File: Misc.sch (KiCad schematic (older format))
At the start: 22 parts, among them U3 PCF8523TK, U4 TLV70218DBV, U5 CDCE913PW, U7 LM75BDP, U8 LM75BDP, X1 32768, X2 20MHz

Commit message: Switch resistors to 0402
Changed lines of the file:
@@
 	5000 2000 4900 2000
 Wire Wire Line
-	4900 2000 4900 2100
-Wire Wire Line
-	4900 2100 4900 2200
+	4900 2000 4900 2200
 Wire Wire Line
 	5000 2100 4900 2100
@@
 $EndComp
 Wire Wire Line
-	2000 1500 2100 1500
-Wire Wire Line
-	2100 1500 2450 1500
-Wire Wire Line
-	2450 1500 2800 1500
-Wire Wire Line
-	2800 1500 3150 1500
-Wire Wire Line
-	3150 1500 5000 1500
+	2000 1500 5000 1500
 $Comp
 L C-0402 C?
@@
 $EndComp
 Wire Wire Line
-	3800 1600 4300 1600
-Wire Wire Line
-	4300 1600 5000 1600
+	3800 1600 5000 1600
 Wire Wire Line
 	3800 1600 3800 1700
@@
 	6100 3900 6200 3900
 Wire Wire Line
-	6200 3900 6200 4000
-Wire Wire Line
-	6200 4000 6200 4100
+	6200 3900 6200 4100
 Wire Wire Line
 	6200 4000 6100 4000
@@
 $EndComp
 Wire Wire Line
-	4300 3800 4600 3800
-Wire Wire Line
-	4600 3800 5100 3800
+	4300 3800 5100 3800
 $Comp
 L GND #PWR169
@@
 	3600 3900 3500 3900
 Wire Wire Line
-	3500 3900 3500 3800
-Wire Wire Line
-	3000 3800 3100 3800
-Wire Wire Line
-	3100 3800 3400 3800
-Wire Wire Line
-	3400 3800 3500 3800
-Wire Wire Line
-	3500 3800 3600 3800
+	3500 3800 3500 3900
+Wire Wire Line
+	3000 3800 3600 3800
 Connection ~ 3500 3800
 Text GLabel 3000 3800 0    50   Input ~ 0
@@
 	3400 3800 3400 4300
 Wire Wire Line
-	3400 4300 5000 4300
+	5000 4300 3400 4300
 Wire Wire Line
 	5000 3900 5100 3900
@@
 	4600 4150 4600 4100
 Wire Wire Line
-	5000 4300 5000 4000
-Wire Wire Line
-	5000 4000 5000 3900
+	5000 3900 5000 4300
 $Comp
 L LM75BDP U7
@@
 P3V3_AUX
 Wire Wire Line
-	4700 4800 4800 4800
-Wire Wire Line
-	4800 4800 5200 4800
+	4700 4800 5200 4800
 Text HLabel 1600 2500 0    50   BiDi ~ 0
 SDA_S0
@@
 	1600 2500 2400 2500
 Wire Wire Line
-	2400 2500 2400 3400
-Wire Wire Line
-	2400 3400 2400 4900
-Wire Wire Line
-	2400 4900 2400 6200
-Wire Wire Line
-	2300 2600 2300 3500
-Wire Wire Line
-	2300 3500 2300 5000
-Wire Wire Line
-	2300 5000 2300 6300
+	2400 2500 2400 6200
+Wire Wire Line
+	2300 2600 2300 6300
 Wire Wire Line
 	2300 2600 1600 2600
@@
 $EndComp
 Wire Wire Line
-	5100 5100 5100 5200
-Wire Wire Line
-	5100 5200 5100 5300
-Wire Wire Line
-	5100 5300 5100 5400
-Wire Wire Line
-	5100 5400 5100 5500
+	5100 5100 5100 5500
 Wire Wire Line
 	5100 5100 5200 5100
@@
 P3V3_AUX
 Wire Wire Line
-	4700 6100 4800 6100
-Wire Wire Line
-	4800 6100 5100 6100
-Wire Wire Line
-	5100 6100 5200 6100
+	4700 6100 5200 6100
 Wire Wire Line
 	2400 6200 5200 6200
@@
 	5200 6500 5100 6500
 Wire Wire Line
-	5100 6500 5100 6600
-Wire Wire Line
-	5100 6600 5100 6700
-Wire Wire Line
-	5100 6700 5100 6800
+	5100 6500 5100 6800
 $Comp
 L GND #PWR176
@@
 	6600 3100 6100 3100
 Wire Wire Line
-	6800 3100 7200 3100
-Wire Wire Line
-	7200 3100 7400 3100
+	6800 3100 7400 3100
 $Comp
 L R-0402 R89
@@
 $EndComp
 Wire Wire Line
-	6800 3200 6900 3200
-Wire Wire Line
-	6900 3200 7400 3200
+	6800 3200 7400 3200
 Wire Wire Line
 	6600 3200 6100 3200

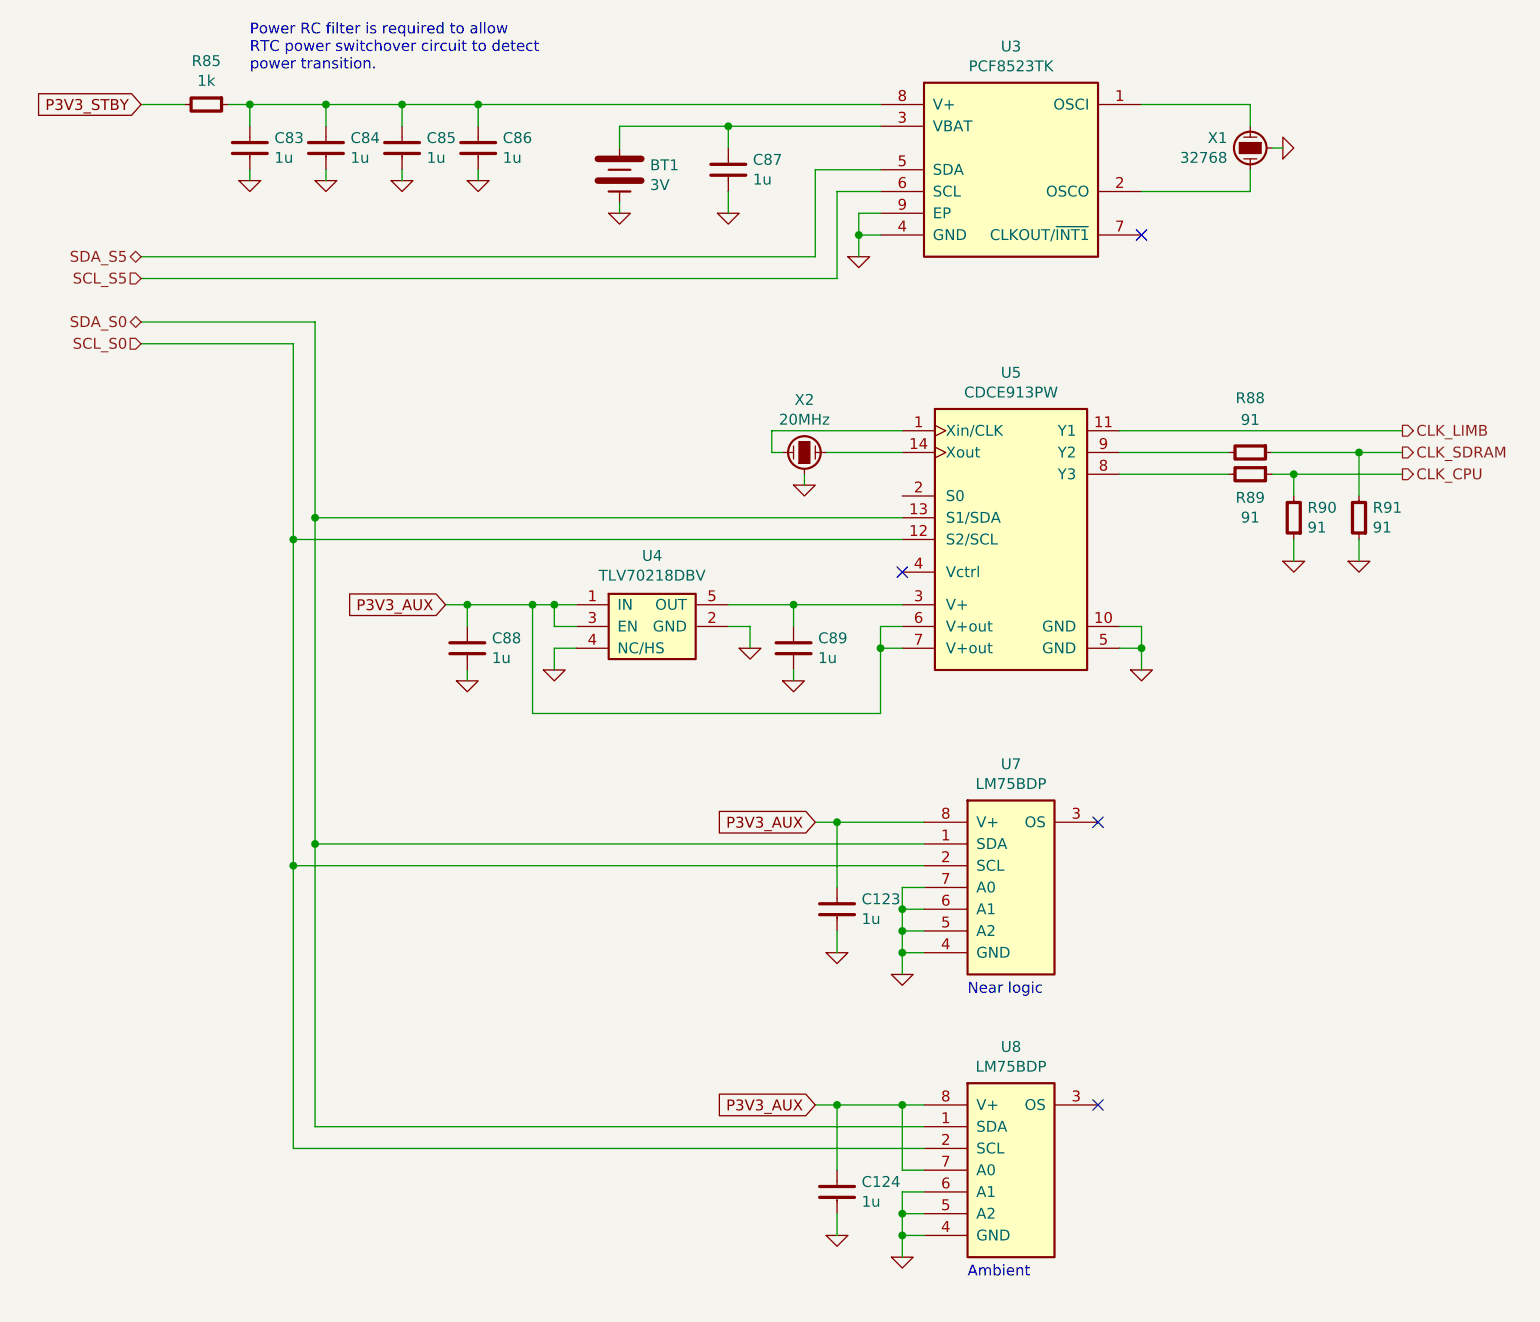
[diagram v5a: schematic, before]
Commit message: Gather and assign all I2C addresses
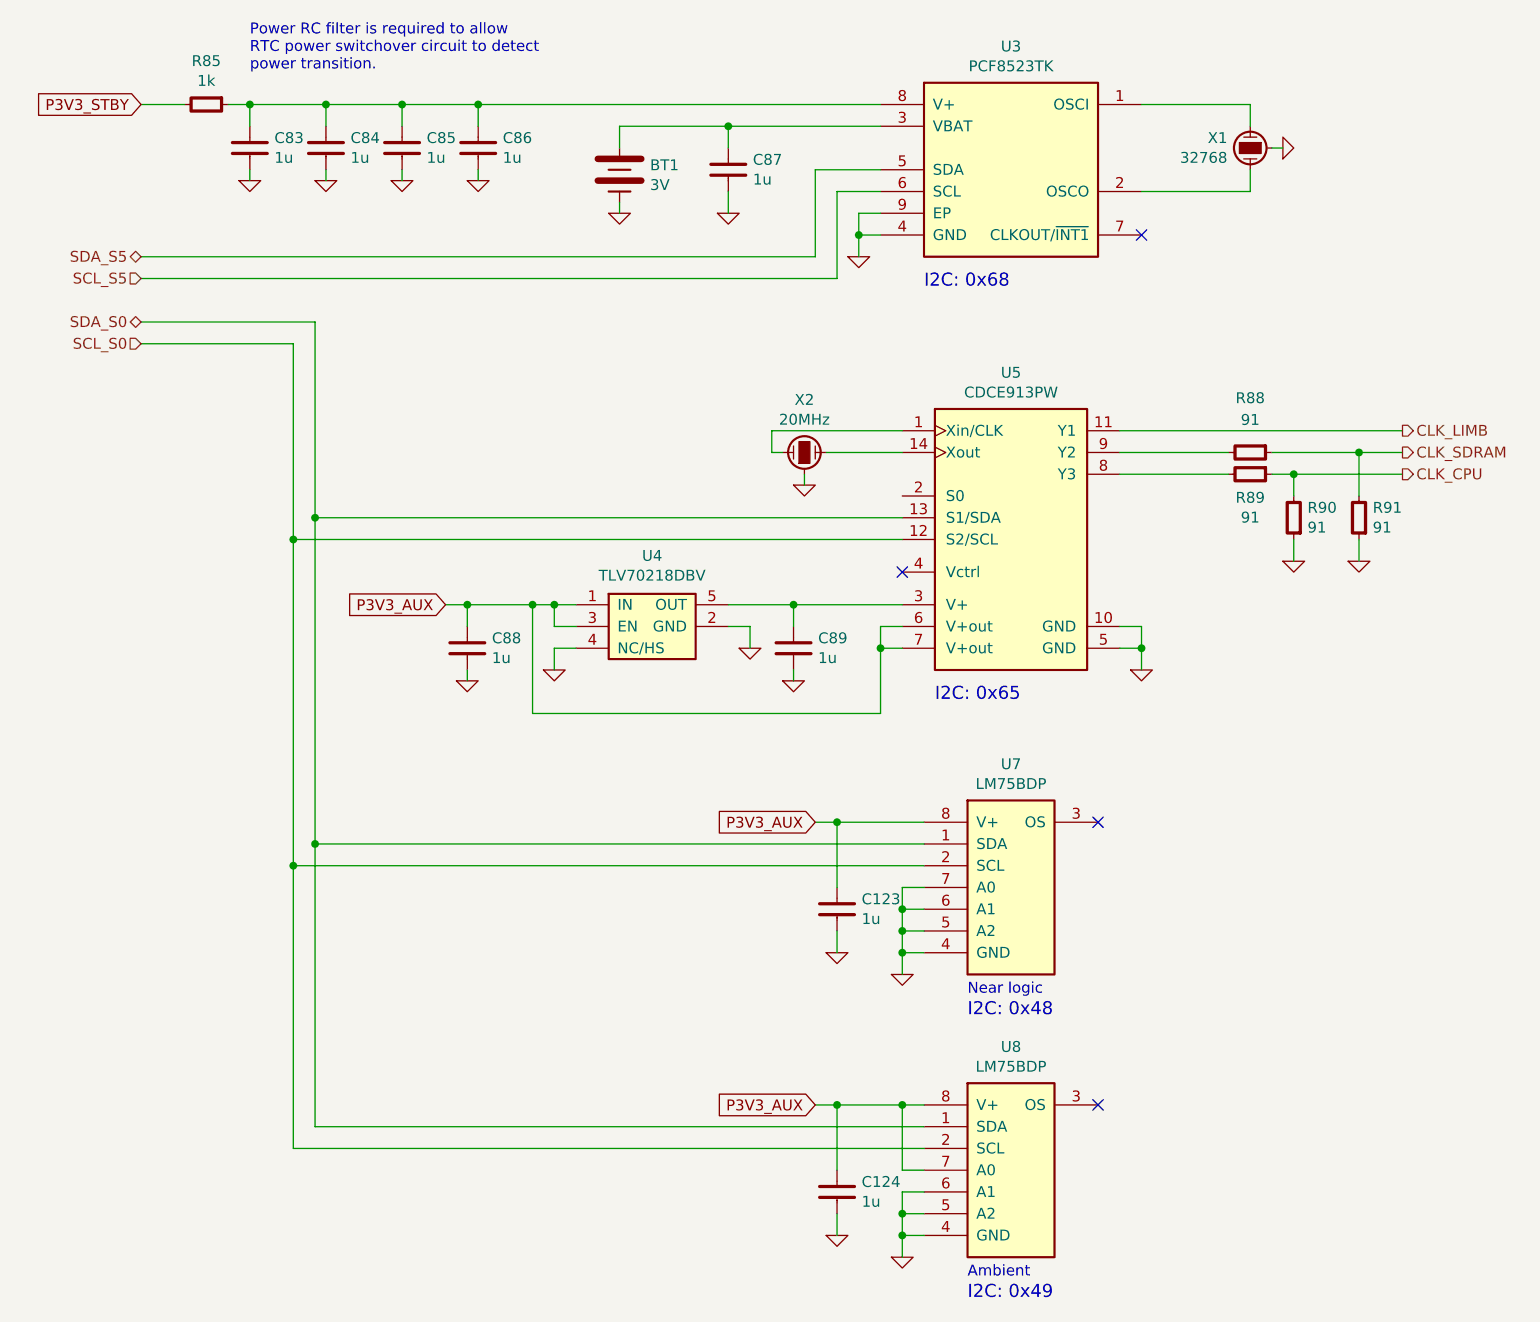
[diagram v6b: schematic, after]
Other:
- note added: "I2C: 0x48"
- note added: "I2C: 0x49"
- note added: "I2C: 0x65"
- note added: "I2C: 0x68"
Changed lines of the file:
@@
 $Descr A 11000 8500
 encoding utf-8
-Sheet 8 10
+Sheet 7 10
 Title "Miscellaneous peripherals"
 Date "2016-08-05"
@@
 	3600 3900 3500 3900
 Wire Wire Line
-	3500 3800 3500 3900
+	3500 3900 3500 3800
 Wire Wire Line
 	3000 3800 3600 3800
@@
 	3400 3800 3400 4300
 Wire Wire Line
-	5000 4300 3400 4300
+	3400 4300 5000 4300
 Wire Wire Line
 	5000 3900 5100 3900
@@
 	4600 4150 4600 4100
 Wire Wire Line
-	5000 3900 5000 4300
+	5000 4300 5000 3900
 $Comp
 L LM75BDP U7
@@
 Text Notes 5400 5600 0    50   ~ 0
 Near logic
+Text Notes 5200 2350 0    60   ~ 0
+I2C: 0x68
+Text Notes 5250 4250 0    60   ~ 0
+I2C: 0x65
+Text Notes 5400 5700 0    60   ~ 0
+I2C: 0x48
+Text Notes 5400 7000 0    60   ~ 0
+I2C: 0x49
 $EndSCHEMATC

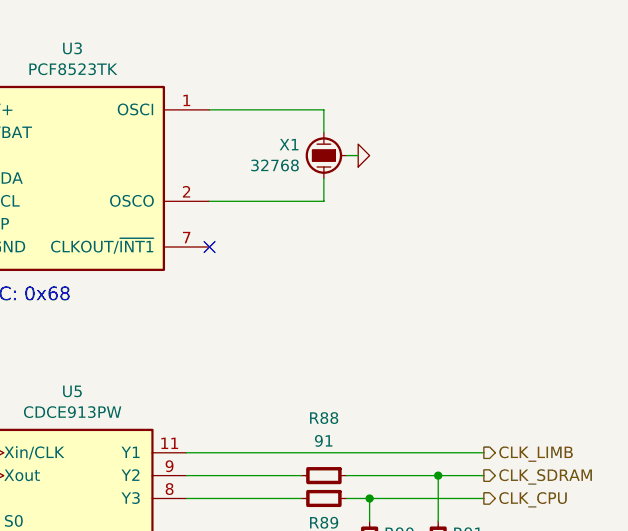
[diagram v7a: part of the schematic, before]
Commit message: Connect RTC alarm interrupt
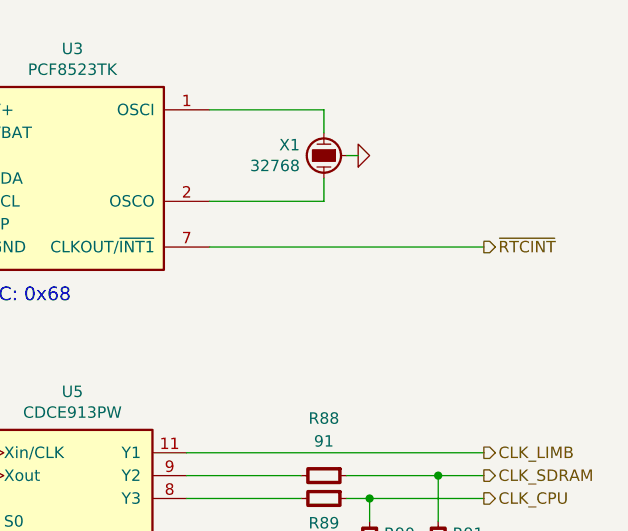
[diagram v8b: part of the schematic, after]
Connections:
- net ~RTCINT: now reaches U3.7 (CLKOUT/~INT1)
- no-connect marks 4 -> 3
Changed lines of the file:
@@
 	1    0    0    -1
 $EndComp
-NoConn ~ 6200 2100
 Wire Wire Line
 	6200 1900 6700 1900
@@
 Text Notes 5400 7000 0    60   ~ 0
 I2C: 0x49
+Text HLabel 7400 2100 2    50   Output ~ 0
+~RTCINT
+Wire Wire Line
+	7400 2100 6200 2100
 $EndSCHEMATC
